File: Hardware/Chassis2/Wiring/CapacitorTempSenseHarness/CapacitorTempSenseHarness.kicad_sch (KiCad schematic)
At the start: 4 parts, among them J1 455-2266-ND

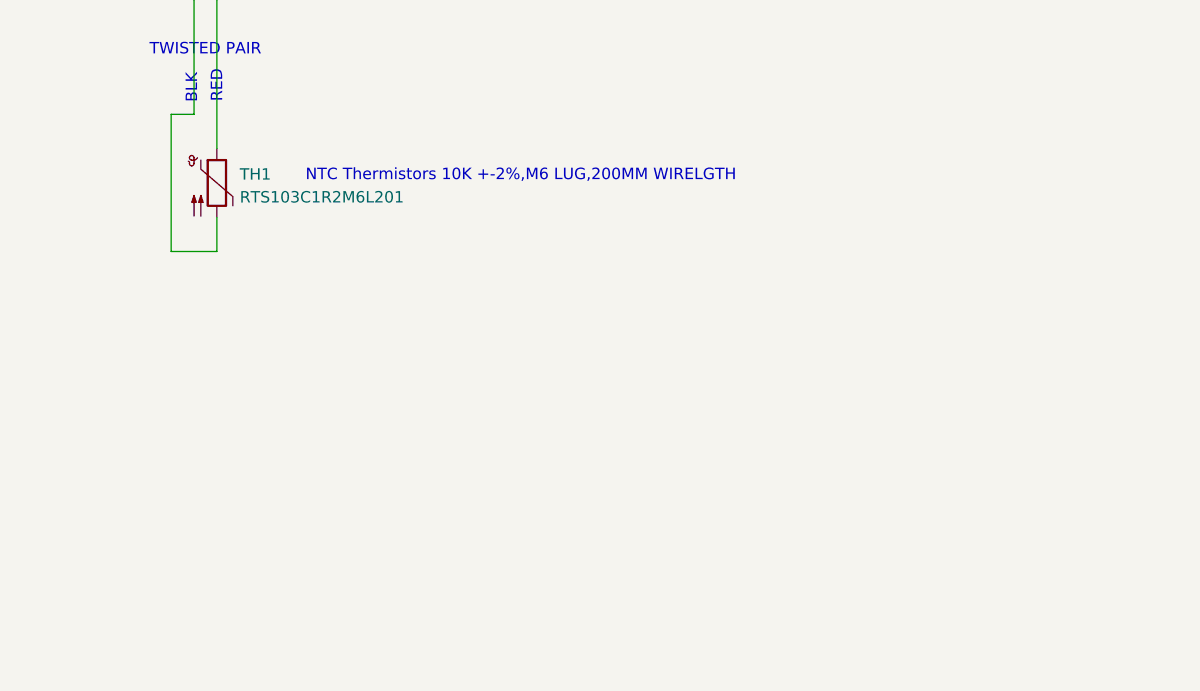
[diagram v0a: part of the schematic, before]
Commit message: Wire harness BOMs from KiCad, board BOM re-exports, tool follows new layouts
- Four harnesses (GDVS, TSIGBT x2, CS x4, TSBCM) with per-chassis Qty
- Board BOMs move to project dirs; discovery prefers root CSV, strips
  library prefixes from footprints, reads KiCad 10 exports
- Mech list down to chassis hardware; IGBT moved to Mouser vendor
- Harness parts leave MechanicalBOM.txt (455-1135-1-ND=SXH-001T-P0.6,
  BC5011CT-ND stray cap, TSW/LA37S600/0022011042/0008500113)
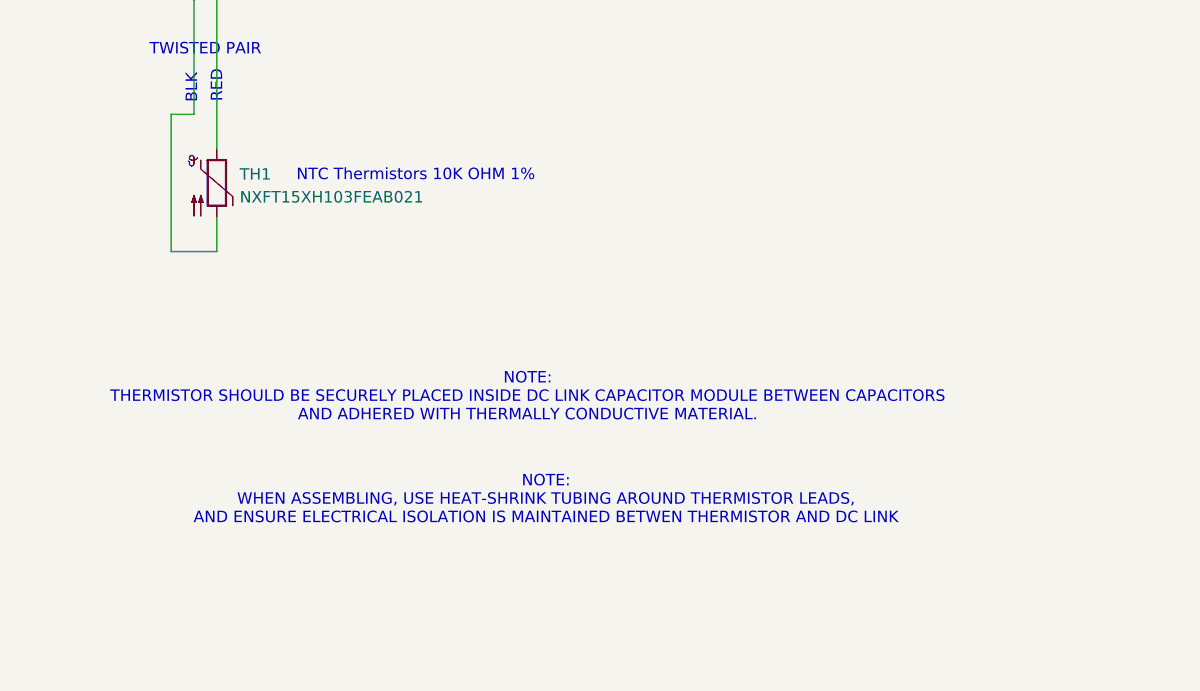
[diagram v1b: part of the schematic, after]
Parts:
- TH1: value RTS103C1R2M6L201 -> NXFT15XH103FEAB021
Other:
- note added: "NOTE: THERMISTOR SHOULD BE SECURELY PLACED INSIDE DC LINK CAPACITOR MODULE BETWEEN CAPACITORS AND ADHERED WITH THERMALLY CONDUCTIVE MATERIAL."
- note added: "NOTE: WHEN ASSEMBLING, USE HEAT-SHRINK TUBING AROUND THERMISTOR LEADS, AND ENSURE ELECTRICAL ISOLATION IS MAINTAINED BETWEN THERMISTOR AND DC LINK"
- note added: "NTC Thermistors 10K OHM 1%"
- note removed: "NTC Thermistors 10K +-2%,M6 LUG,200MM WIRELGTH"
- title: Open Inverter Platform - IGBT Temperature Wiring Harness -> Open Inverter Platform - Capacitor Temp Sense Wiring Harness
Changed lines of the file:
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@@
 	(paper "USLetter")
 	(title_block
-		(title "Open Inverter Platform - IGBT Temperature Wiring Harness")
+		(title "Open Inverter Platform - Capacitor Temp Sense Wiring Harness")
 		(date "2026-07-16")
 		(rev "A")
 		(company "Corzine Lab, University of California, Santa Cruz")
 		(comment 1 "Prepared by Thomas Liao")
-		(comment 2 "HW-C2-WH-TSIGBT")
-	)
-	(text "NTC Thermistors 10K +-2%,M6 LUG,200MM WIRELGTH "
-		(exclude_from_sim no)
-		(at 65.532 71.628 0)
+		(comment 2 "HW-C2-WH-TSBCM")
+	)
+	(text "NOTE:\nTHERMISTOR SHOULD BE SECURELY PLACED INSIDE DC LINK CAPACITOR MODULE BETWEEN CAPACITORS\nAND ADHERED WITH THERMALLY CONDUCTIVE MATERIAL."
+		(exclude_from_sim no)
+		(at 66.294 96.266 0)
+		(effects
+			(font
+				(size 1.27 1.27)
+			)
+		)
+	)
+	(text "NTC Thermistors 10K OHM 1% "
+		(exclude_from_sim no)
+		(at 53.848 71.628 0)
+		(effects
+			(font
+				(size 1.27 1.27)
+			)
+		)
+	)
+	(text "NOTE:\nWHEN ASSEMBLING, USE HEAT-SHRINK TUBING AROUND THERMISTOR LEADS,\nAND ENSURE ELECTRICAL ISOLATION IS MAINTAINED BETWEN THERMISTOR AND DC LINK"
+		(exclude_from_sim no)
+		(at 68.326 107.696 0)
 		(effects
 			(font
@@
 		)
 		(instances
-			(project "TempSenseHarness"
+			(project "CapacitorTempSenseHarness"
 				(path "/2365f093-f079-4cf2-9926-0ba7dd4b2726"
 					(reference "Z2")
@@
 		)
 		(instances
-			(project "TempSenseHarness"
+			(project "CapacitorTempSenseHarness"
 				(path "/2365f093-f079-4cf2-9926-0ba7dd4b2726"
 					(reference "J1")
@@
 			)
 		)
-		(property "Value" "RTS103C1R2M6L201"
+		(property "Value" "NXFT15XH103FEAB021"
 			(at 34.29 73.9774 0)
 			(show_name no)
@@
 		)
 		(instances
-			(project "TempSenseHarness"
+			(project "CapacitorTempSenseHarness"
 				(path "/2365f093-f079-4cf2-9926-0ba7dd4b2726"
 					(reference "TH1")
@@
 		)
 		(instances
-			(project "TempSenseHarness"
+			(project "CapacitorTempSenseHarness"
 				(path "/2365f093-f079-4cf2-9926-0ba7dd4b2726"
 					(reference "Z1")

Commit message: Rename Open Inverter Platform to InverterGen5, schematic PDF export, tidy variants
- Title blocks renamed to InverterGen5 in all harness schematics
- regen now re-exports schematic PDFs for boards and harnesses too
- Spares variants live under FabricationData/BOMs/Variants/
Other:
- title: Open Inverter Platform - Capacitor Temp Sense Wiring Harness -> InverterGen5 - Capacitor Temp Sense Wiring Harness
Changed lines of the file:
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@@
 	(paper "USLetter")
 	(title_block
-		(title "Open Inverter Platform - Capacitor Temp Sense Wiring Harness")
+		(title "InverterGen5 - Capacitor Temp Sense Wiring Harness")
 		(date "2026-07-16")
 		(rev "A")
